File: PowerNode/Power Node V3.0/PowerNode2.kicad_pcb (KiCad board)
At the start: 2 copper layers, 78.4 x 64.8 mm, 58 parts, among them IC1 CD4511B, IC4 ACS712xLCTR-30A, IC5 74HC595N, IC7 CD4511B

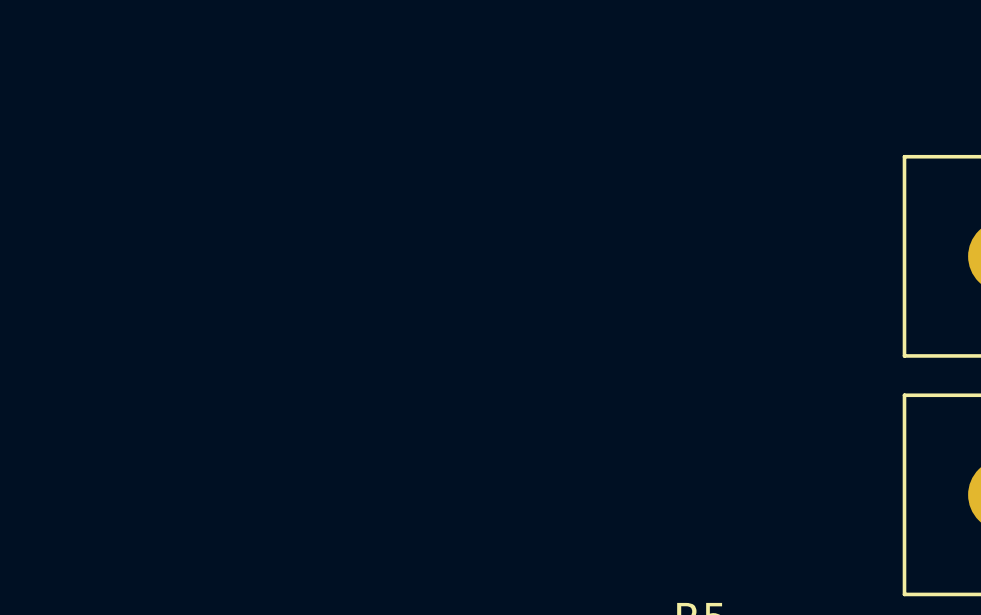
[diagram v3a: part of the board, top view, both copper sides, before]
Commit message: PN3: added pull-down resistors for DP1 and QH*1
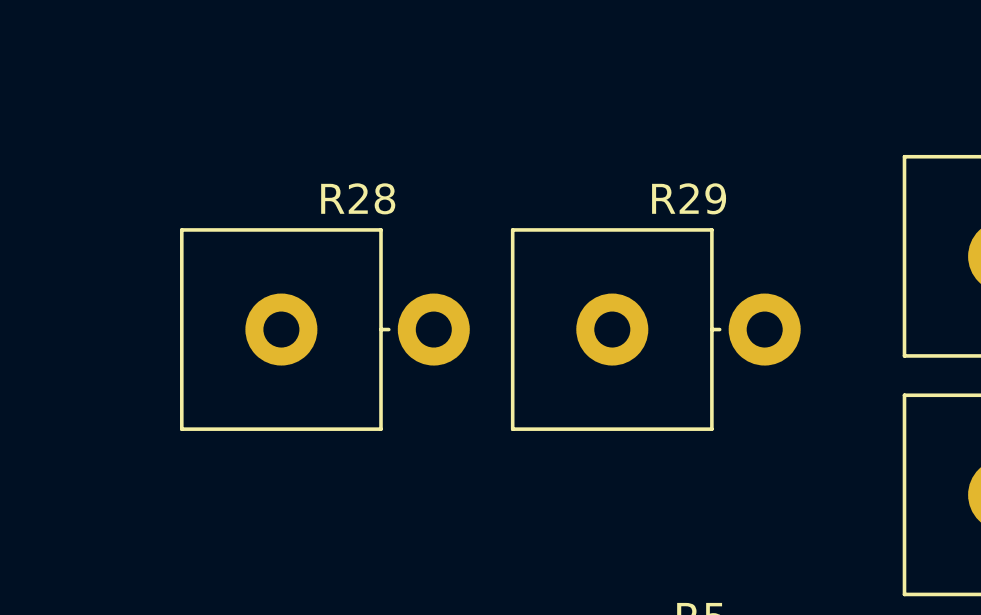
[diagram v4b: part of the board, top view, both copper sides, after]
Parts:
- added R28: 10k, Resistor_THT:R_Axial_Power_L20.0mm_W6.4mm_P5.08mm_Vertical, F.Cu at (135.9, 50.8)
- added R29: 10k, Resistor_THT:R_Axial_Power_L20.0mm_W6.4mm_P5.08mm_Vertical, F.Cu at (146.9, 50.8)
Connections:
- C5 pad 1: /VHI -> /VMEAS
- IC4 pad 1: GND -> Net-(GNDHIOUT1-Pad1)
- IC4 pad 2: GND -> Net-(GNDHIOUT1-Pad1)
- IC4 pad 3: Net-(GNDHIOUT1-Pad1) -> GND
- IC4 pad 4: Net-(GNDHIOUT1-Pad1) -> GND
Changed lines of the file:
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@@
     (tracks 658)
     (zones 0)
-    (modules 58)
+    (modules 60)
     (nets 69)
   )
@@
     (add_net "Net-(R6-Pad2)")
     (add_net Vdd)
+  )
+  (module Resistor_THT:R_Axial_Power_L20.0mm_W6.4mm_P5.08mm_Vertical (layer Top)
+    (at 146.92 50.8)
+    (descr "Resistor, Axial_Power series, Axial, Vertical, pin pitch=5.08mm, 4W, length*width*height=20*6.4*6.4mm^3, http://cdn-reichelt.de/documents/datenblatt/B400/5WAXIAL_9WAXIAL_11WAXIAL_17WAXIAL%23YAG.pdf")
+    (tags "Resistor Axial_Power series Axial Vertical pin pitch 5.08mm 4W length 20mm width 6.4mm height 6.4mm")
+    (fp_text reference R29 (at 2.54 -4.32) (layer F.SilkS)
+      (effects (font (size 1 1) (thickness 0.15)))
+    )
+    (fp_text value 10k (at 2.54 4.32) (layer F.Fab)
+      (effects (font (size 1 1) (thickness 0.15)))
+    )
+    (fp_text user %R (at 0 -1.7) (layer F.Fab)
+      (effects (font (size 1 1) (thickness 0.15)))
+    )
+    (fp_line (start 6.53 -3.45) (end -3.45 -3.45) (layer F.CrtYd) (width 0.05))
+    (fp_line (start 6.53 3.45) (end 6.53 -3.45) (layer F.CrtYd) (width 0.05))
+    (fp_line (start -3.45 3.45) (end 6.53 3.45) (layer F.CrtYd) (width 0.05))
+    (fp_line (start -3.45 -3.45) (end -3.45 3.45) (layer F.CrtYd) (width 0.05))
+    (fp_line (start 3.32 0) (end 3.58 0) (layer F.SilkS) (width 0.12))
+    (fp_line (start 3.32 -3.32) (end -3.32 -3.32) (layer F.SilkS) (width 0.12))
+    (fp_line (start 3.32 3.32) (end 3.32 -3.32) (layer F.SilkS) (width 0.12))
+    (fp_line (start -3.32 3.32) (end 3.32 3.32) (layer F.SilkS) (width 0.12))
+    (fp_line (start -3.32 -3.32) (end -3.32 3.32) (layer F.SilkS) (width 0.12))
+    (fp_line (start 0 0) (end 5.08 0) (layer F.Fab) (width 0.1))
+    (fp_line (start 3.2 -3.2) (end -3.2 -3.2) (layer F.Fab) (width 0.1))
+    (fp_line (start 3.2 3.2) (end 3.2 -3.2) (layer F.Fab) (width 0.1))
+    (fp_line (start -3.2 3.2) (end 3.2 3.2) (layer F.Fab) (width 0.1))
+    (fp_line (start -3.2 -3.2) (end -3.2 3.2) (layer F.Fab) (width 0.1))
+    (pad 2 thru_hole oval (at 5.08 0) (size 2.4 2.4) (drill 1.2) (layers *.Cu *.Mask)
+      (net 64 "Net-(LED1-Pad6)"))
+    (pad 1 thru_hole circle (at 0 0) (size 2.4 2.4) (drill 1.2) (layers *.Cu *.Mask)
+      (net 58 GND))
+    (model ${KISYS3DMOD}/Resistor_THT.3dshapes/R_Axial_Power_L20.0mm_W6.4mm_P5.08mm_Vertical.wrl
+      (at (xyz 0 0 0))
+      (scale (xyz 1 1 1))
+      (rotate (xyz 0 0 0))
+    )
+  )
+  (module Resistor_THT:R_Axial_Power_L20.0mm_W6.4mm_P5.08mm_Vertical (layer Top)
+    (at 135.89 50.8)
+    (descr "Resistor, Axial_Power series, Axial, Vertical, pin pitch=5.08mm, 4W, length*width*height=20*6.4*6.4mm^3, http://cdn-reichelt.de/documents/datenblatt/B400/5WAXIAL_9WAXIAL_11WAXIAL_17WAXIAL%23YAG.pdf")
+    (tags "Resistor Axial_Power series Axial Vertical pin pitch 5.08mm 4W length 20mm width 6.4mm height 6.4mm")
+    (fp_text reference R28 (at 2.54 -4.32) (layer F.SilkS)
+      (effects (font (size 1 1) (thickness 0.15)))
+    )
+    (fp_text value 10k (at 2.54 4.32) (layer F.Fab)
+      (effects (font (size 1 1) (thickness 0.15)))
+    )
+    (fp_text user %R (at 0 -1.7) (layer F.Fab)
+      (effects (font (size 1 1) (thickness 0.15)))
+    )
+    (fp_line (start 6.53 -3.45) (end -3.45 -3.45) (layer F.CrtYd) (width 0.05))
+    (fp_line (start 6.53 3.45) (end 6.53 -3.45) (layer F.CrtYd) (width 0.05))
+    (fp_line (start -3.45 3.45) (end 6.53 3.45) (layer F.CrtYd) (width 0.05))
+    (fp_line (start -3.45 -3.45) (end -3.45 3.45) (layer F.CrtYd) (width 0.05))
+    (fp_line (start 3.32 0) (end 3.58 0) (layer F.SilkS) (width 0.12))
+    (fp_line (start 3.32 -3.32) (end -3.32 -3.32) (layer F.SilkS) (width 0.12))
+    (fp_line (start 3.32 3.32) (end 3.32 -3.32) (layer F.SilkS) (width 0.12))
+    (fp_line (start -3.32 3.32) (end 3.32 3.32) (layer F.SilkS) (width 0.12))
+    (fp_line (start -3.32 -3.32) (end -3.32 3.32) (layer F.SilkS) (width 0.12))
+    (fp_line (start 0 0) (end 5.08 0) (layer F.Fab) (width 0.1))
+    (fp_line (start 3.2 -3.2) (end -3.2 -3.2) (layer F.Fab) (width 0.1))
+    (fp_line (start 3.2 3.2) (end 3.2 -3.2) (layer F.Fab) (width 0.1))
+    (fp_line (start -3.2 3.2) (end 3.2 3.2) (layer F.Fab) (width 0.1))
+    (fp_line (start -3.2 -3.2) (end -3.2 3.2) (layer F.Fab) (width 0.1))
+    (pad 2 thru_hole oval (at 5.08 0) (size 2.4 2.4) (drill 1.2) (layers *.Cu *.Mask)
+      (net 28 "Net-(IC5-Pad9)"))
+    (pad 1 thru_hole circle (at 0 0) (size 2.4 2.4) (drill 1.2) (layers *.Cu *.Mask)
+      (net 58 GND))
+    (model ${KISYS3DMOD}/Resistor_THT.3dshapes/R_Axial_Power_L20.0mm_W6.4mm_P5.08mm_Vertical.wrl
+      (at (xyz 0 0 0))
+      (scale (xyz 1 1 1))
+      (rotate (xyz 0 0 0))
+    )
   )
   (module Capacitor_THT:CP_Radial_D16.0mm_P7.50mm (layer Top)
@@
       (net 58 GND))
     (pad 1 thru_hole rect (at 0 0) (size 2.4 2.4) (drill 1.2) (layers *.Cu *.Mask)
-      (net 68 /VHI))
+      (net 65 /VMEAS))
     (model ${KISYS3DMOD}/Capacitor_THT.3dshapes/CP_Radial_D16.0mm_P7.50mm.wrl
       (at (xyz 0 0 0))
@@
       (net 58 GND))
     (pad 4 smd roundrect (at -2.475 1.905 270) (size 1.95 0.6) (layers Top F.Paste F.Mask) (roundrect_rratio 0.25)
+      (net 58 GND))
+    (pad 3 smd roundrect (at -2.475 0.635 270) (size 1.95 0.6) (layers Top F.Paste F.Mask) (roundrect_rratio 0.25)
+      (net 58 GND))
+    (pad 2 smd roundrect (at -2.475 -0.635 270) (size 1.95 0.6) (layers Top F.Paste F.Mask) (roundrect_rratio 0.25)
       (net 52 "Net-(GNDHIOUT1-Pad1)"))
-    (pad 3 smd roundrect (at -2.475 0.635 270) (size 1.95 0.6) (layers Top F.Paste F.Mask) (roundrect_rratio 0.25)
+    (pad 1 smd roundrect (at -2.475 -1.905 270) (size 1.95 0.6) (layers Top F.Paste F.Mask) (roundrect_rratio 0.25)
       (net 52 "Net-(GNDHIOUT1-Pad1)"))
-    (pad 2 smd roundrect (at -2.475 -0.635 270) (size 1.95 0.6) (layers Top F.Paste F.Mask) (roundrect_rratio 0.25)
-      (net 58 GND))
-    (pad 1 smd roundrect (at -2.475 -1.905 270) (size 1.95 0.6) (layers Top F.Paste F.Mask) (roundrect_rratio 0.25)
-      (net 58 GND))
     (model ${KISYS3DMOD}/Package_SO.3dshapes/SOIC-8_3.9x4.9mm_P1.27mm.wrl
       (at (xyz 0 0 0))

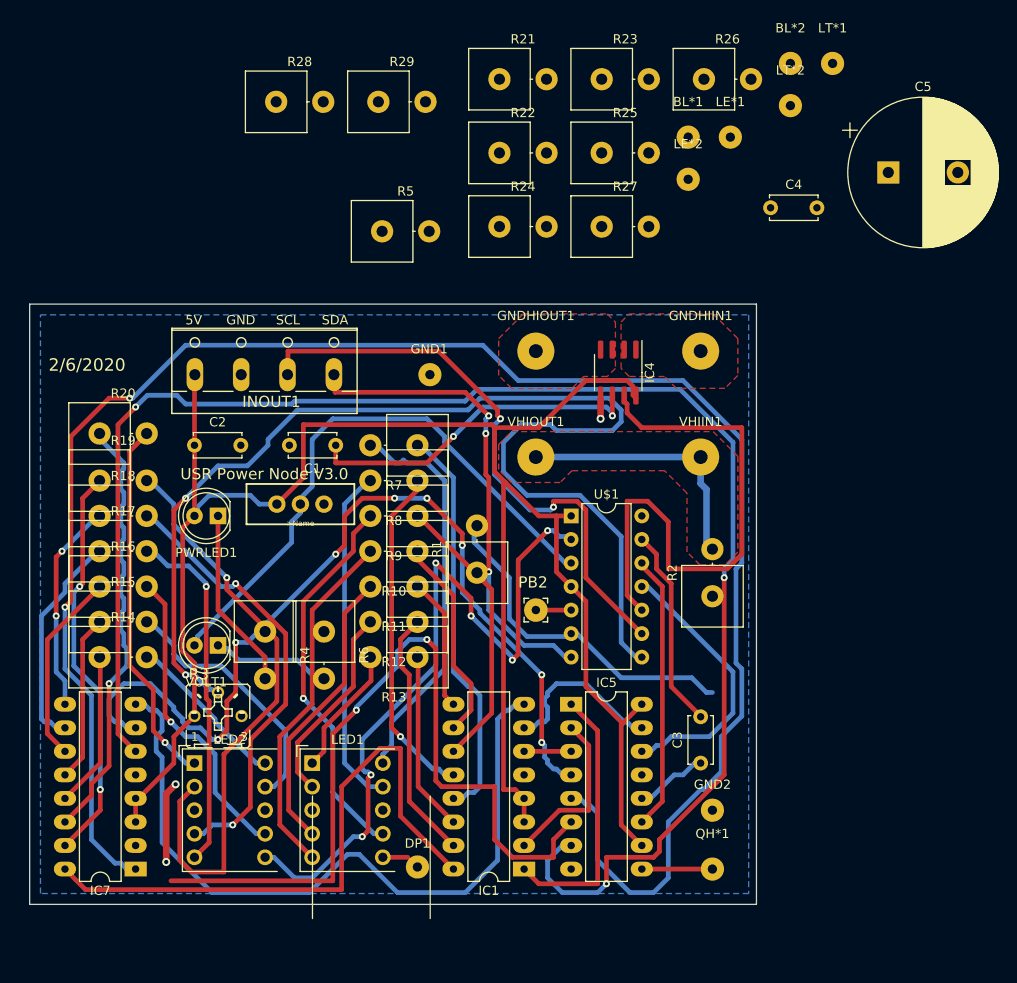
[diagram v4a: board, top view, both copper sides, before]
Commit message: PN3: updated footprints and 3D models
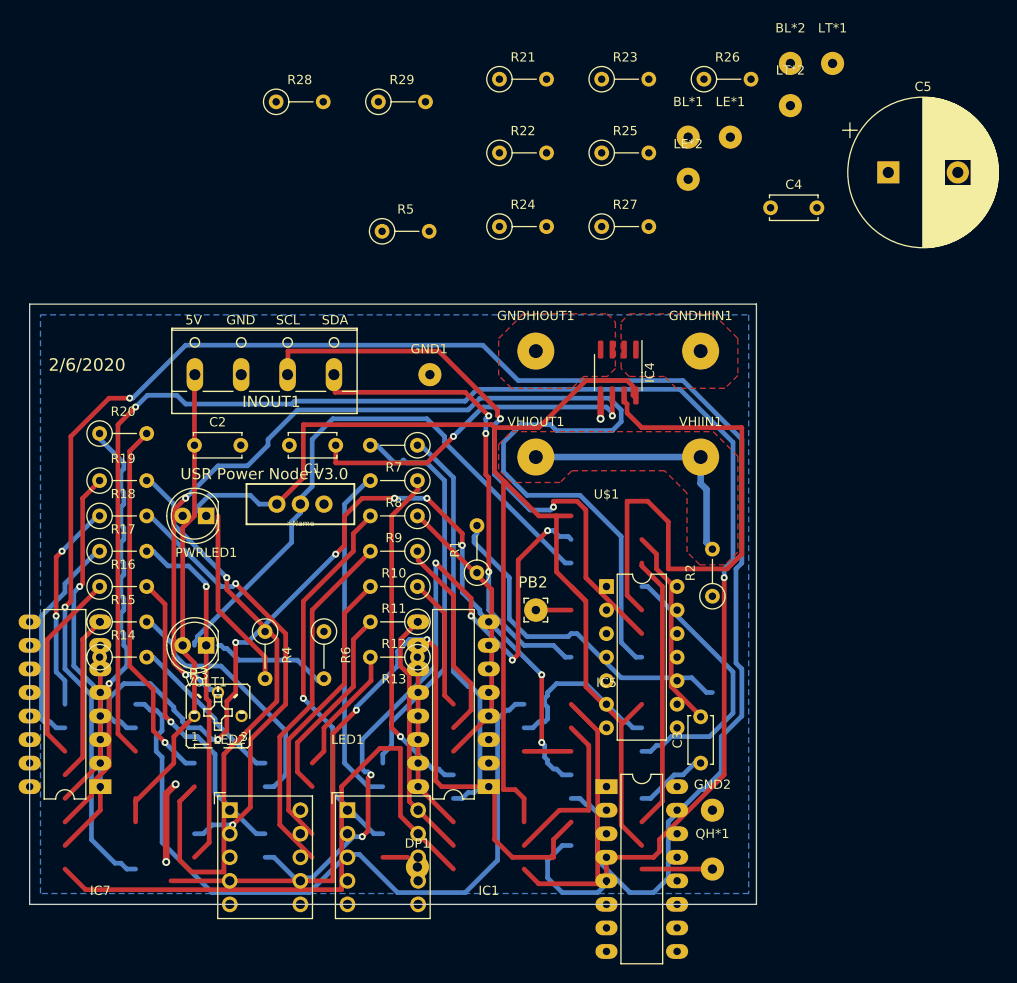
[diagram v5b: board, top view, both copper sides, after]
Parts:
- R1, R10, R11, R12, R13, R14, R15, R16, R17, R18, R19, R2, R20, R21, R22, R23, R24, R25, R26, R27, R28, R29, R4, R5, R6, R7, R8, R9: footprint Resistor_THT:R_Axial_Power_L20.0mm_W6.4mm_P5.08mm_Vertical -> Resistor_THT:R_Axial_DIN0207_L6.3mm_D2.5mm_P5.08mm_Vertical
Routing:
- net Net-(LED1-Pad9): track 37.0 -> 102.4 mm
- net Vdd: track 65.3 -> 0.00 mm
- net /VCC: track 208.0 -> 210.3 mm

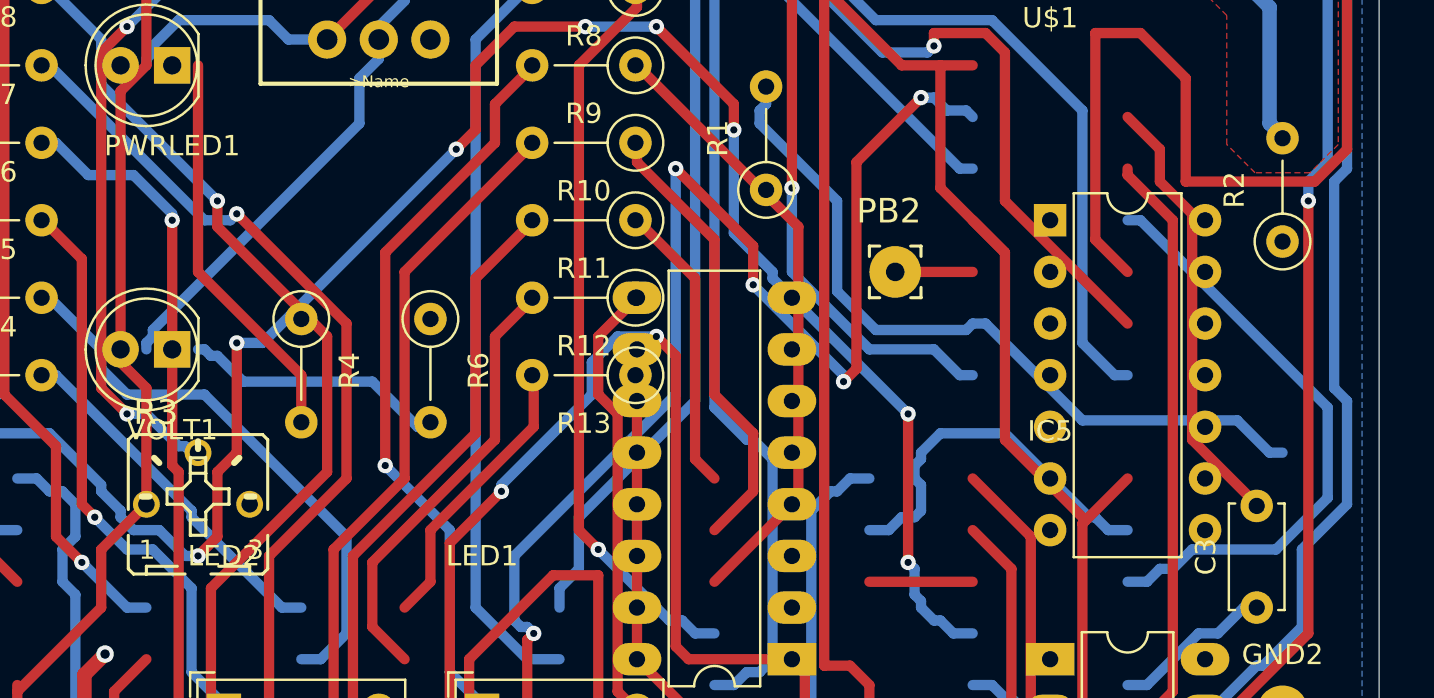
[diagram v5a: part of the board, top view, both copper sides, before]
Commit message: PN3: updated board and footprints
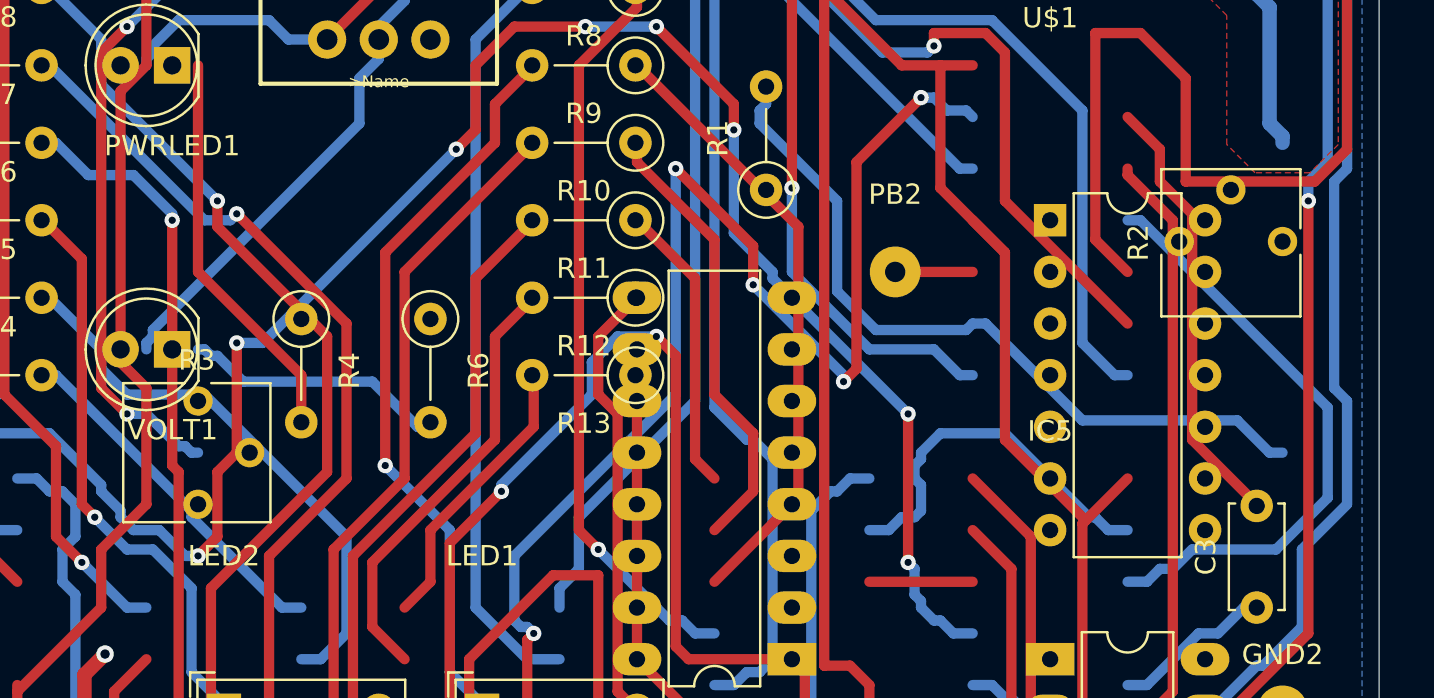
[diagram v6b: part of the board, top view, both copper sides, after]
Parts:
- PB2: footprint PowerNode2:2,54_0,9 -> Connector_Wire:SolderWirePad_1x01_Drill1mm
- R2: value 1.2Meg -> TRIM_US-B25P; footprint Resistor_THT:R_Axial_DIN0207_L6.3mm_D2.5mm_P5.08mm_Vertical -> Potentiometer_THT:Potentiometer_Vishay_T73YP_Vertical
- R3: footprint PowerNode2:B25P -> Potentiometer_THT:Potentiometer_Vishay_T73YP_Vertical
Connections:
- net /BL*1 renamed /BL'1
- net /BL*2 renamed /BL'2
- net /LE*1 renamed /LE'1
- net /LE*2 renamed /LE'2
- net /LT*1 renamed /LT'1
- net /LT*2 renamed /LT'2
- net Net-(IC5-Pad9) renamed /QH'
- net Net-(LED1-Pad1) renamed /g1
- net Net-(LED1-Pad10) renamed /a1
- net Net-(LED1-Pad2) renamed /f1
- net Net-(LED1-Pad4) renamed /e1
- net Net-(LED1-Pad5) renamed /d1
- net Net-(LED1-Pad6) renamed /DP1
- net Net-(LED1-Pad7) renamed /c1
- net Net-(LED1-Pad9) renamed /b1
- net Net-(LED2-Pad1) renamed /g2
- net Net-(LED2-Pad10) renamed /a2
- net Net-(LED2-Pad2) renamed /f2
- net Net-(LED2-Pad4) renamed /e2
- net Net-(LED2-Pad5) renamed /d2
- net Net-(LED2-Pad6) renamed /DP2
- net Net-(LED2-Pad7) renamed /c2
- net Net-(LED2-Pad9) renamed /b2
- net Net-(PB2-Pad1) renamed /PB2
- C1 pad 2: GND -> Vss
- C2 pad 2: GND -> Vss
- C4 pad 2: GND -> Vss
- C5 pad 2: GND -> Vss
- GND1 pad 1: GND -> Vss
- GND2 pad 1: GND -> Vss
- GNDHIIN1 pad 1: GND -> Vss
- IC1 pad 8: GND -> Vss
- IC4 pad 3: GND -> Vss
- IC4 pad 4: GND -> Vss
- IC4 pad 5: GND -> Vss
- IC5 pad 13: GND -> Vss
- IC5 pad 8: GND -> Vss
- IC7 pad 8: GND -> Vss
- INOUT1 pad 2: GND -> Vss
- LED1 pad 3: GND -> Vss
- LED1 pad 8: GND -> Vss
- LED2 pad 3: GND -> Vss
- LED2 pad 8: GND -> Vss
- R2 pad 1: /VMEAS -> /VHI
- R2 pad 2: /VHI -> /VMEAS
- R25 pad 1: GND -> Vss
- R26 pad 1: GND -> Vss
- R28 pad 1: GND -> Vss
- R29 pad 1: GND -> Vss
- R3 pad 3: GND -> Vss
- R4 pad 1: GND -> Vss
- R6 pad 1: GND -> Vss
- S1 pad 3: GND -> Vss
- U$1 pad 14: GND -> Vss
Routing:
- net Net-(LED2-Pad6): track 0.00 -> 79.4 mm
- net /DP2: track 79.4 -> 0.00 mm
- net Net-(LED1-Pad9): track 0.00 -> 65.3 mm
- net /b1: track 102.4 -> 37.0 mm
- net Net-(LED2-Pad2): track 0.00 -> 64.5 mm
- net /f2: track 64.5 -> 0.00 mm
- net Net-(LED1-Pad10): track 0.00 -> 43.0 mm
- net /a1: track 43.0 -> 0.00 mm
- net Net-(LED1-Pad7): track 0.00 -> 41.4 mm
- net /c1: track 41.4 -> 0.00 mm
- net Net-(LED1-Pad5): track 0.00 -> 38.5 mm
- net /d1: track 38.5 -> 0.00 mm
- net Net-(LED2-Pad5): track 0.00 -> 38.1 mm
- net /d2: track 38.1 -> 0.00 mm
- net Net-(LED2-Pad7): track 0.00 -> 33.2 mm
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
